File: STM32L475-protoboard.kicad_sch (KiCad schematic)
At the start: 79 parts, among them J1 USB_HEADER, J10 BOOT_MODE, J11 PAD_PB4, J12 PAD_PB5, J13 PAD_PC4, J14 PAD_PC5, J15 PAD_GND, J16 Conn_02x20_Odd_Even, J2 USB_B_Micro, J3 DCin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

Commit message: misc routing
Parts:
- removed TP1: TestPoint, TestPoint:TestPoint_Pad_D2.0mm, symbol Connector:TestPoint
- added C25, C26, C27, C28: DNP, Capacitor_SMD:C_0805_2012Metric_Pad1.18x1.45mm_HandSolder, symbol Device:C_Small
- added J17: 3v3-hdr, Connector_PinHeader_2.54mm:PinHeader_1x02_P2.54mm_Vertical, symbol Connector:Conn_01x02_Pin
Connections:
- net +3V3: now also J17.2 (Pin_2)
- net GND: now also C25.1, C26.1, C27.1, C28.1, J17.1 (Pin_1)
- net PA6: now also J16.19 (Pin_19); no longer J16.27 (Pin_27)
- net PA7: now also J16.17 (Pin_17); no longer J16.25 (Pin_25)
- net PC0: now also J16.27 (Pin_27), C27.2; no longer J16.23 (Pin_23)
- net PC1: now also J16.25 (Pin_25), C28.2; no longer J16.21 (Pin_21)
- net PC2: now also J16.23 (Pin_23), C26.2; no longer J16.19 (Pin_19)
- net PC3: now also J16.21 (Pin_21), C25.2; no longer J16.17 (Pin_17)
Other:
- note added: "-W5500-moduulin oikea paikka! -USB ID pin -USB VBUS pin -tsekkaa DFU-homma"
- note removed: "-USB ID pin + pull-up datalinjaan -tsekkaa DFU-homma -A/D:t (väh 3 + LPF..) + kaikki DAC-linjat"
- note removed: "I2C 2k2-pullupeilla"
- moved on the sheet: C20, C21

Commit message: to be continued
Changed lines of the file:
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@@
   )
   (text "-W5500-moduulin oikea paikka!\n-USB ID pin\n-USB VBUS pin\n-tsekkaa DFU-homma"
-    (at 99.06 -5.08 0)
+    (at 218.44 184.15 0)
     (effects (font (size 2.5 2.5) (thickness 0.6) bold) (justify left bottom))
   )

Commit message: almost there
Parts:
- removed J4: STLINK, symbol Connector_Generic:Conn_02x05_Odd_Even
- removed J7: PAD_PA9_USART1_TX, Connector_Wire:SolderWirePad_1x01_SMD_1x2mm, symbol Connector:Conn_01x01_Male
- removed J8: PAD_PA10_USART1_RX, Connector_Wire:SolderWirePad_1x01_SMD_1x2mm, symbol Connector:Conn_01x01_Male
- added C29, C30: 1uF, Capacitor_SMD:C_0603_1608Metric, symbol Device:C_Small
- added J4: PAD_PA8_OTG_FS_SOF, Connector_Wire:SolderWirePad_1x01_SMD_1x2mm, symbol Connector:Conn_01x01_Male
- added JP2, JP3: J, Jumper:SolderJumper-2_P1.3mm_Open_RoundedPad1.0x1.5mm, symbol Jumper:Jumper_2_Open
- added R17, R18, R19, R20, R22: 0, Resistor_SMD:R_0603_1608Metric_Pad0.98x0.95mm_HandSolder, symbol Device:R
- added U4: XC6206PxxxMR, Package_TO_SOT_SMD:SOT-23-3, symbol Regulator_Linear:XC6206PxxxMR
- C10: footprint Capacitor_SMD:C_0805_2012Metric_Pad1.18x1.45mm_HandSolder -> Capacitor_SMD:C_0603_1608Metric; LCSC (none) -> C14663
- C11, C14, C15, C19, C2, C24, C3, C6, C7: footprint Capacitor_SMD:C_0805_2012Metric -> Capacitor_SMD:C_0603_1608Metric; LCSC (none) -> C14663
- C12, C13, C8: LCSC (none) -> C1634
- C16, C17: LCSC (none) -> C38523
- C18, C22, C23, C4, C5, C9: footprint Capacitor_SMD:C_0805_2012Metric_Pad1.18x1.45mm_HandSolder -> Capacitor_SMD:C_0805_2012Metric
- C20, C21, C25, C26, C27, C28: footprint Capacitor_SMD:C_0805_2012Metric_Pad1.18x1.45mm_HandSolder -> Capacitor_SMD:C_1206_3216Metric_Pad1.33x1.80mm_HandSolder
- Card2: LCSC (none) -> C393941
- D4, D5: footprint LED_SMD:LED_0805_2012Metric -> LED_SMD:LED_0603_1608Metric; LCSC (none) -> C2286
- J2: LCSC (none) -> C136000
- R1, R5: footprint Resistor_SMD:R_0603_1608Metric_Pad0.98x0.95mm_HandSolder -> Resistor_SMD:R_0603_1608Metric; LCSC (none) -> C23138
- R10, R12, R13, R14, R4, R9: footprint Resistor_SMD:R_0603_1608Metric_Pad0.98x0.95mm_HandSolder -> Resistor_SMD:R_0603_1608Metric; LCSC (none) -> C25804
- R11, R15, R2: footprint Resistor_SMD:R_0603_1608Metric_Pad0.98x0.95mm_HandSolder -> Resistor_SMD:R_0603_1608Metric; LCSC (none) -> C22843
- R16: LCSC (none) -> C21189
- R3: LCSC (none) -> C21190
- R6, R7: footprint Resistor_SMD:R_0603_1608Metric_Pad0.98x0.95mm_HandSolder -> Resistor_SMD:R_0603_1608Metric; LCSC (none) -> C23345
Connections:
- net +3V3: now also JP3.2 (B); no longer J5.1 (Pin_1)
- net +VDC: now also C2.1, C4.1, C5.1, C6.1, C7.1, D1.1 (K), D2.1 (K), J16.3 (Pin_3), U2.3 (VI), R22.2; no longer C1.1, D1.2 (A), F2.1
- net GND: now also C29.1, C30.1, R17.1, R18.1, R19.1, R20.1, U4.1 (GND)
- net PA9: now also JP2.2 (B)
- net VBUS: now also C29.2, U4.3 (VI); no longer J16.3 (Pin_3)
- net PA8: now reaches U3.41 (PA8)
- net PA8: now also J4.1 (Pin_1)
- net at H5.1: now also R19.2
- net at J5.2 (Pin_2): now also R22.1
- net at H3.1: now also R17.2
- net at H4.1: now also R18.2
- net at H6.1: now also R20.2
- new net: C30.2, JP2.1 (A), U4.2 (VO)
- new net: C1.1, D1.2 (A), F2.1
- new net: J5.1 (Pin_1), JP3.1 (A)
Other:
- note added: "-varmista vielä W5500-moduulin paikka! -varmista kiinnitysreikien paikka -DRC check (JLC:n säännöt)"
- note added: "USB VBUS detect"
- note removed: "-W5500-moduulin oikea paikka! -USB ID pin -USB VBUS pin -tsekkaa DFU-homma"
- note removed: "JLC DRC RULES!"
- moved on the sheet: C14, C18, C20, C21, C22, C23, C24, C25, C26, C27, C28, C3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

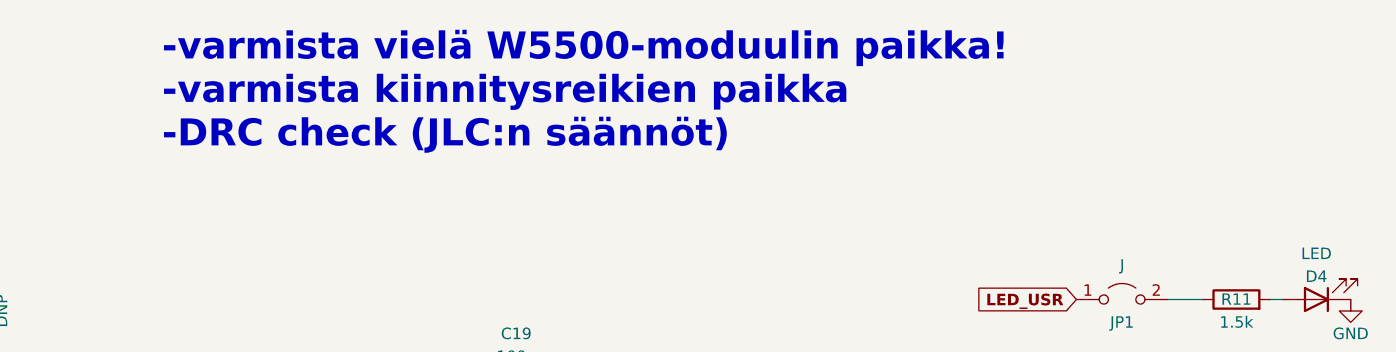
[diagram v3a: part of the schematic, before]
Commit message: mounting holes
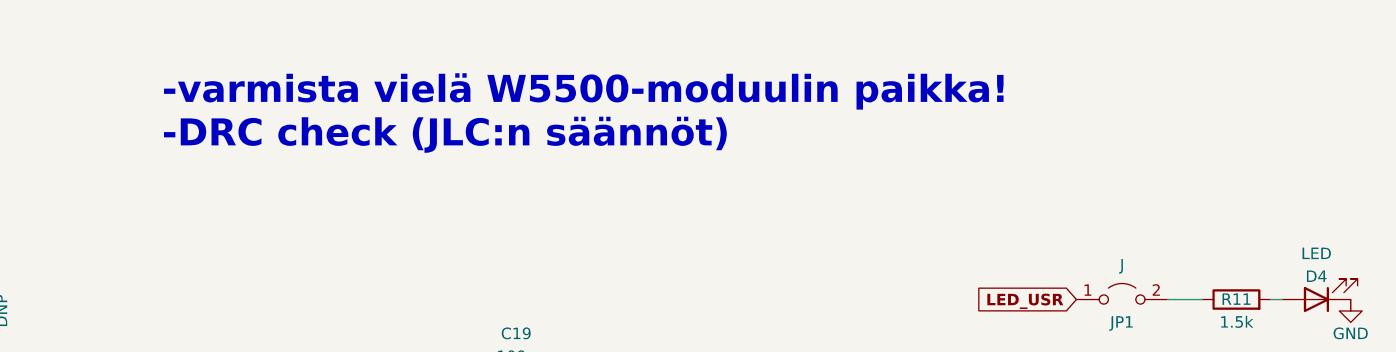
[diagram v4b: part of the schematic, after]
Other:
- note added: "-varmista vielä W5500-moduulin paikka! -DRC check (JLC:n säännöt)"
- note removed: "-varmista vielä W5500-moduulin paikka! -varmista kiinnitysreikien paikka -DRC check (JLC:n säännöt)"
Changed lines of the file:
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@@
     (effects (font (size 2 2) (thickness 0.254) bold) (justify left bottom))
   )
-  (text "-varmista vielä W5500-moduulin paikka!\n-varmista kiinnitysreikien paikka\n-DRC check (JLC:n säännöt)"
+  (text "-varmista vielä W5500-moduulin paikka!\n-DRC check (JLC:n säännöt)"
     (at 104.14 6.35 0)
     (effects (font (size 3 3) (thickness 0.6) bold) (justify left bottom))

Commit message: drc trace separtion checking
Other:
- note added: "-varmista vielä W5500-moduulin paikka! -USB-liitin"
- note removed: "-varmista vielä W5500-moduulin paikka! -DRC check (JLC:n säännöt)"
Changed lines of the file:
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@@
     (effects (font (size 2 2) (thickness 0.254) bold) (justify left bottom))
   )
-  (text "-varmista vielä W5500-moduulin paikka!\n-DRC check (JLC:n säännöt)"
+  (text "-varmista vielä W5500-moduulin paikka!\n-USB-liitin"
     (at 104.14 6.35 0)
     (effects (font (size 3 3) (thickness 0.6) bold) (justify left bottom))

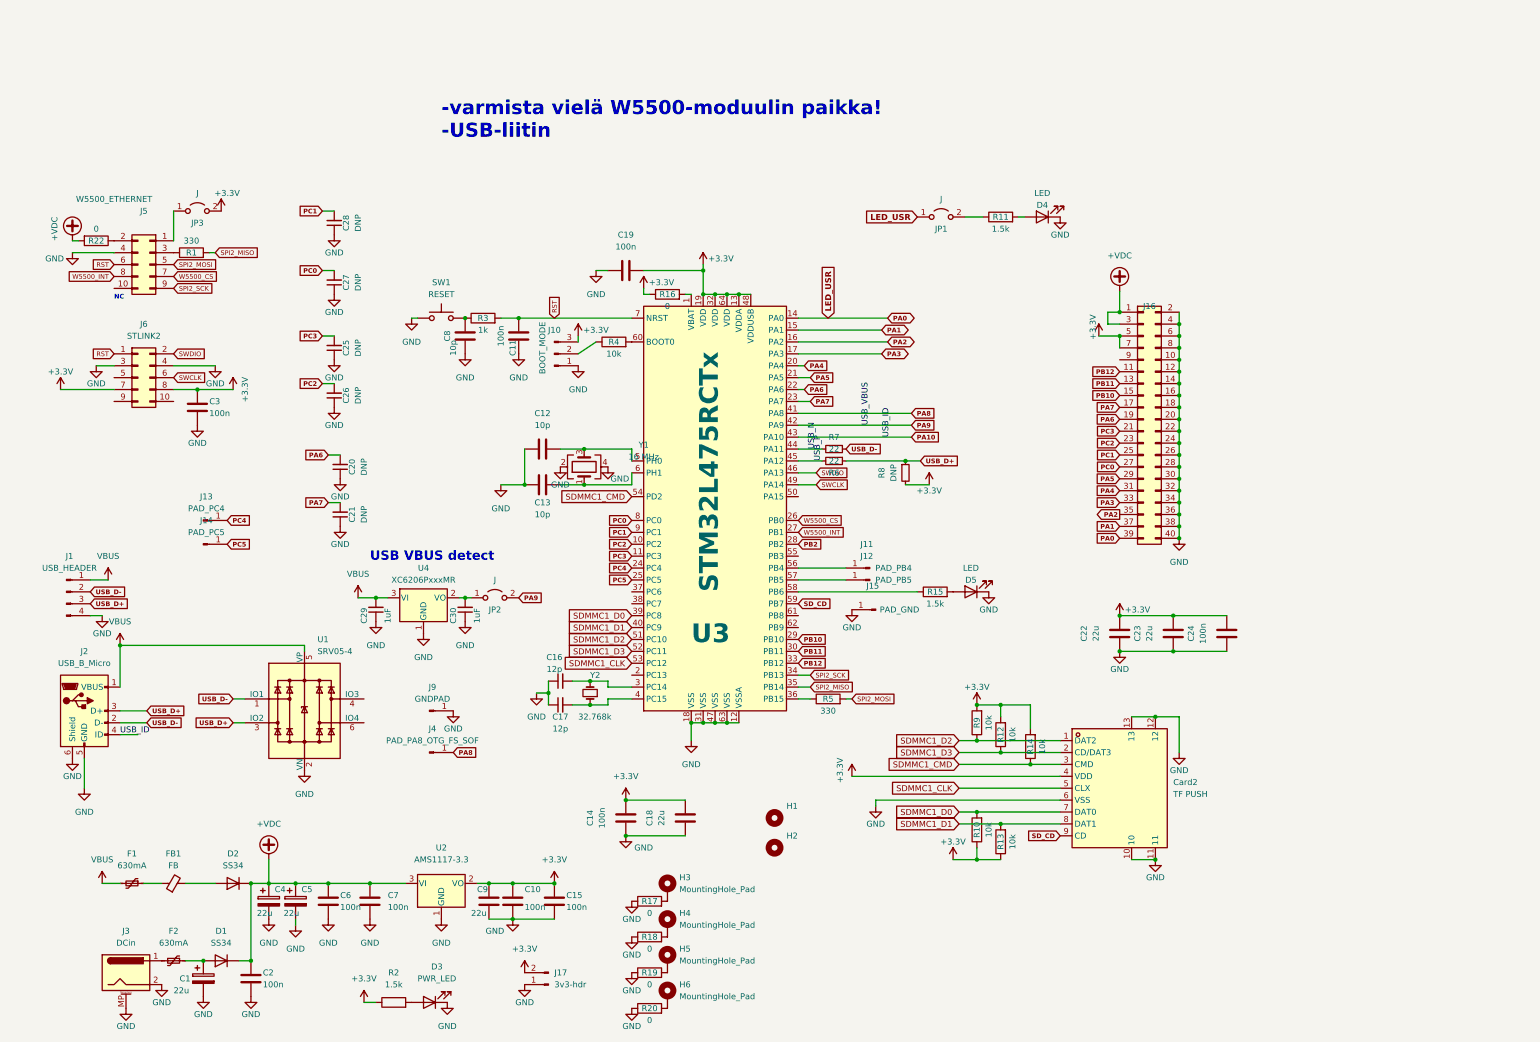
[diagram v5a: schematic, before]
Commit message: micro usb connector change
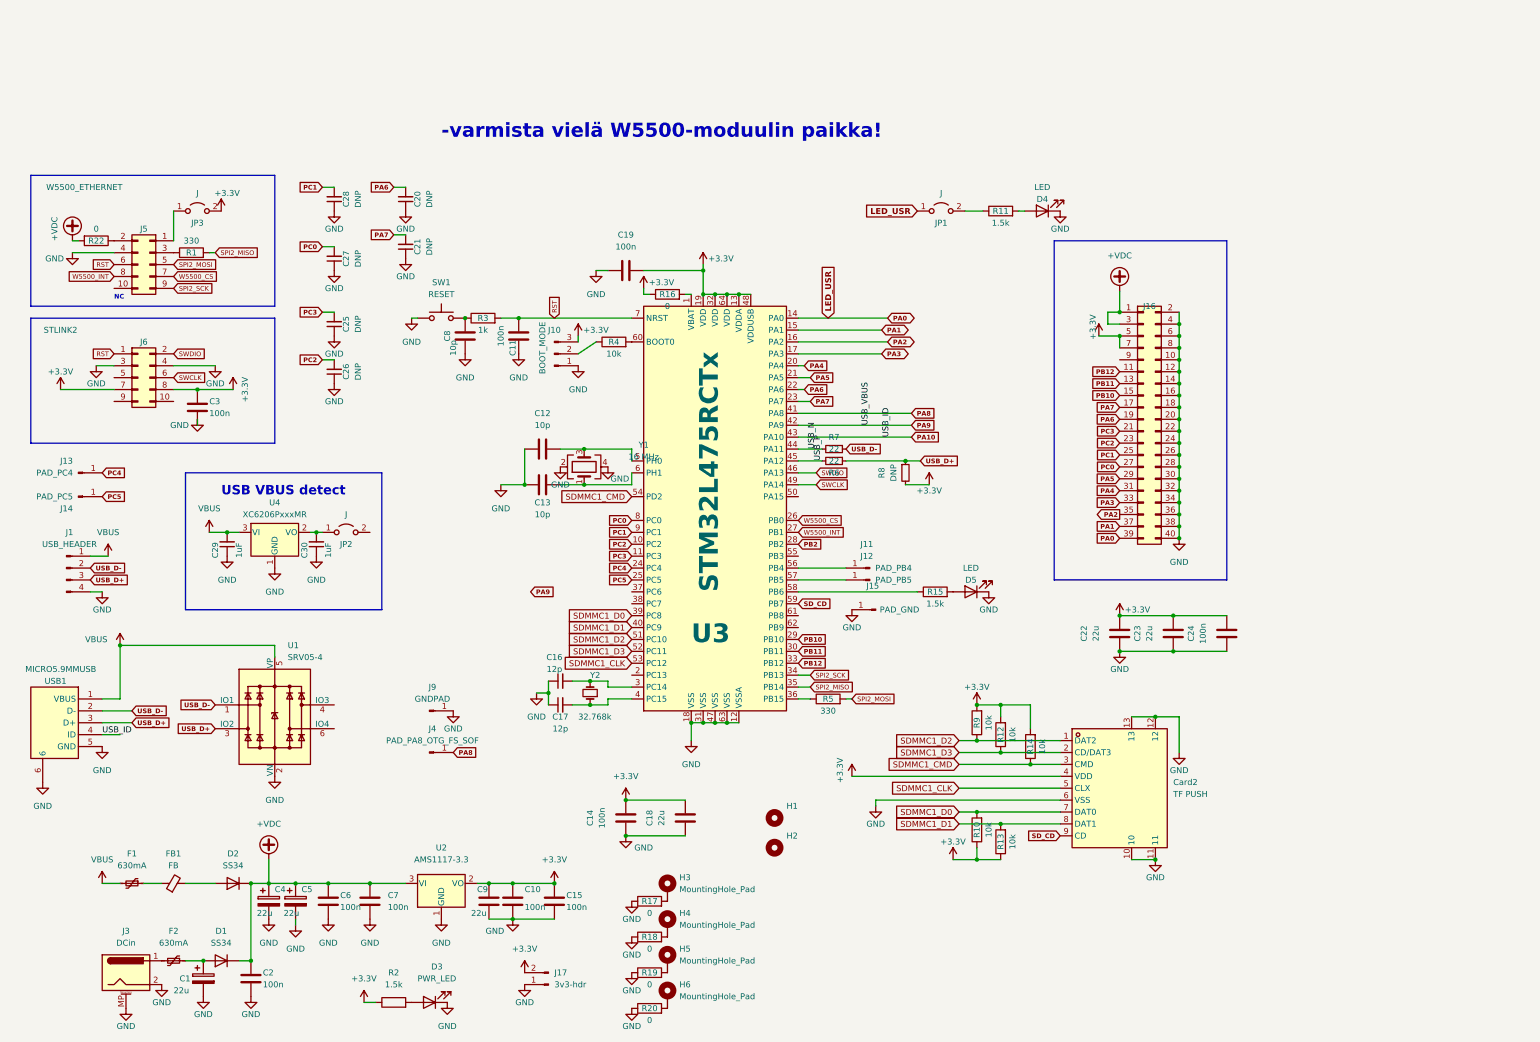
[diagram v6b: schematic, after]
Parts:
- removed J2: USB_B_Micro, Connector_USB:USB_Micro-B_Molex-105017-0001, symbol Connector:USB_B_Micro
- added USB1: MICRO5.9MMUSB, STM32L475-protoboard:MICRO-USB-SMD_5P-P0.65-H-F_MICRO5.9MMUSB, symbol microUSB:MICRO5.9MMUSB
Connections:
- net GND: now also USB1.5 (GND), USB1.6
- net PA10: now also USB1.4 (ID)
- net PA9: no longer JP2.2 (B)
- net USB_D+: now also USB1.3 (D+)
- net USB_D-: now also USB1.2 (D-)
- net VBUS: now also USB1.1 (VBUS)
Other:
- note added: "-varmista vielä W5500-moduulin paikka!"
- note removed: "-varmista vielä W5500-moduulin paikka! -USB-liitin"
- moved on the sheet: C20, C21, C25, C26, C27, C28, C29, C30, D4, J1, J13, J14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

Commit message: schema pdf
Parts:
- U3: value STM32L475RCTx -> STM32L475RCT6
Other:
- note removed: "-varmista vielä W5500-moduulin paikka!"
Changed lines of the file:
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@@
     (effects (font (size 2 2) (thickness 0.254) bold) (justify left bottom))
-  )
-  (text "-varmista vielä W5500-moduulin paikka!" (at 104.14 6.35 0)
-    (effects (font (size 3 3) (thickness 0.6) bold) (justify left bottom))
   )
   (text "NC" (at 34.29 40.64 0)
@@
       (effects (font (size 4 4) bold) (justify left))
     )
-    (property "Value" "STM32L475RCTx" (at 161.29 102.87 90)
+    (property "Value" "STM32L475RCT6" (at 161.29 102.87 90)
       (effects (font (size 4 4) bold) (justify left))
     )
